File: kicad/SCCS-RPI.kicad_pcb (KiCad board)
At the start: 4 copper layers, 228 x 122 mm, 298 parts, among them J1 Conn_Coaxial, J2 12VDC IN, K1 Relay_SPDT, K2 Relay_SPDT, K3 Relay_SPDT, K4 Relay_SPDT, Q1 IRLR7843, Q10 IRLR7843, Q11 IRLR7843, Q12 IRLR7843, Q13 IRLR7843, Q14 IRLR7843, Q15 IRLR7843, Q16 IRLR7843, Q17 2N7000, Q18 2N7000, Q19 2N7000, Q2 IRLR7843, Q20 2N7000, Q3 IRLR7843, Q4 IRLR7843, Q5 IRLR7843, Q6 IRLR7843, Q7 IRLR7843, Q8 IRLR7843, Q9 IRLR7843, SW1 RESET, SW2 BOOT, SW3 RESET, SW4 BOOT, U1 SN74LVC2T45DCUR, U2 AP64501SP-13, U3 PC817, U4 PC817, U5 PC817, U6 PC817

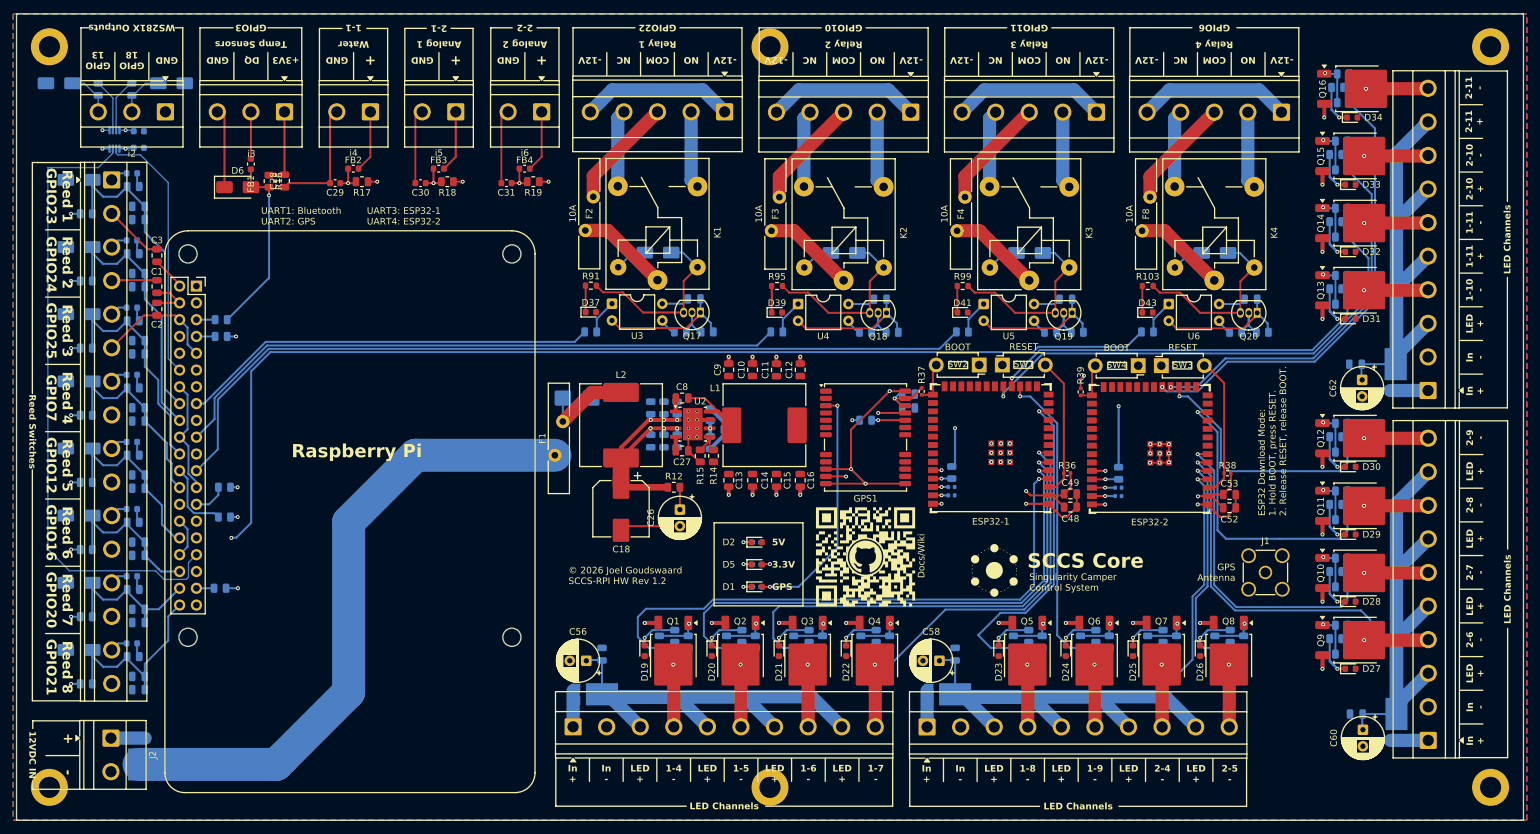
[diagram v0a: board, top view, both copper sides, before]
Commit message: Update SCCS-RPI KiCad design and production files
Add GPS RF ESD and matching (ESD103-B1-02EL, 27nH, 10R, 100nF),
swap the 10A fuses to A16-1000, retune copper zone fills, and
regenerate BOM, positions, netlist, gerbers, and schematics PDF.
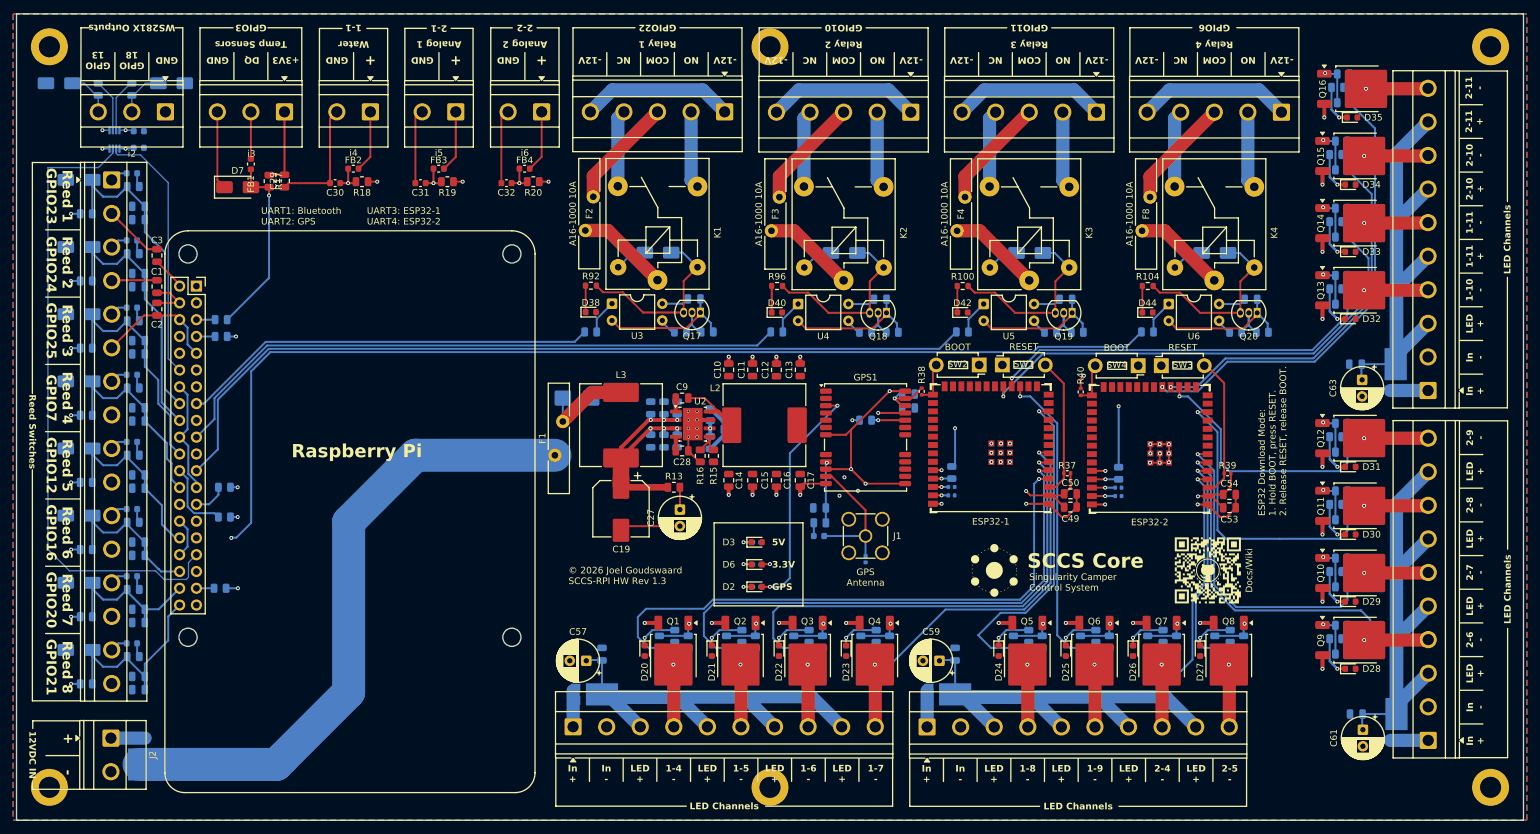
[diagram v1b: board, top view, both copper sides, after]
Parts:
- added C8: 100nF, Capacitor_SMD:C_0805_2012Metric, B.Cu at (322.0, 200.8)
- added D1: ESD103-B1-02EL, Diode_SMD:D_0402_1005Metric, B.Cu at (329.0, 208.5)
- added L1: 27nH, Inductor_SMD:L_0603_1608Metric, B.Cu at (321.9, 205.0)
- added R8: 10R, Resistor_SMD:R_0805_2012Metric, B.Cu at (322.0, 203.0)
- F1, F2, F3, F4, F5: value 10A -> A16-1000 10A
- moved J1 60.8 mm to (329.0, 205.0)
- moved G*** 51.8 mm to (380.8, 210.2)
- renumbered C9 to C10, C10 to C11, C11 to C12, C12 to C13, C13 to C14, C14 to C15, C15 to C16, C16 to C17, C17 to C18, C18 to C19, C19 to C20, C20 to C21, C21 to C22, C22 to C23, C23 to C24, C24 to C25, C25 to C26, C26 to C27, C27 to C28, C28 to C29, C29 to C30, C30 to C31, C31 to C32, C32 to C33, C33 to C34, C34 to C35, C35 to C36, C36 to C37, C37 to C38, C38 to C39, C39 to C40, C40 to C41, C41 to C42, C42 to C43, C43 to C44, C44 to C45, C45 to C46, C46 to C47, C47 to C48, C48 to C49, C49 to C50, C50 to C51, C51 to C52, C52 to C53, C53 to C54, C54 to C55, C55 to C56, C56 to C57, C57 to C58, C58 to C59, C59 to C60, C60 to C61, C61 to C62, C62 to C63, C63 to C64, C64 to C65, C65 to C66, C66 to C67, C67 to C68, C8 to C9, D9 to D10, D10 to D11, D11 to D12, D12 to D13, D13 to D14, D14 to D15, D15 to D16, D16 to D17, D17 to D18, D18 to D19, D1 to D2, D19 to D20, D20 to D21, D21 to D22, D22 to D23, D23 to D24, D24 to D25, D25 to D26, D26 to D27, D27 to D28, D28 to D29, D2 to D3, D29 to D30, D30 to D31, D31 to D32, D32 to D33, D33 to D34, D34 to D35, D35 to D36, D36 to D37, D37 to D38, D38 to D39, D3 to D4, D39 to D40, D40 to D41, D41 to D42, D42 to D43, D43 to D44, D44 to D45, D4 to D5, D5 to D6, D6 to D7, D7 to D8, D8 to D9, L1 to L2, L2 to L3, R9 to R10, R99 to R100, R100 to R101, R101 to R102, R102 to R103, R103 to R104, R104 to R105, R105 to R106, R10 to R11, R11 to R12, R12 to R13, R13 to R14, R14 to R15, R15 to R16, R16 to R17, R17 to R18, R18 to R19, R19 to R20, R20 to R21, R21 to R22, R22 to R23, R23 to R24, R24 to R25, R25 to R26, R26 to R27, R27 to R28, R28 to R29, R29 to R30, R30 to R31, R31 to R32, R32 to R33, R33 to R34, R34 to R35, R35 to R36, R36 to R37, R37 to R38, R38 to R39, R39 to R40, R40 to R41, R41 to R42, R42 to R43, R43 to R44, R44 to R45, R45 to R46, R46 to R47, R47 to R48, R48 to R49, R49 to R50, R50 to R51, R51 to R52, R52 to R53, R53 to R54, R54 to R55, R55 to R56, R56 to R57, R57 to R58, R58 to R59, R59 to R60, R60 to R61, R61 to R62, R62 to R63, R63 to R64, R64 to R65, R65 to R66, R66 to R67, R67 to R68, R68 to R69, R69 to R70, R70 to R71, R71 to R72, R72 to R73, R73 to R74, R74 to R75, R75 to R76, R76 to R77, R77 to R78, R78 to R79, R79 to R80, R80 to R81, R81 to R82, R82 to R83, R83 to R84, R84 to R85, R85 to R86, R86 to R87, R87 to R88, R88 to R89, R8 to R9, R89 to R90, R90 to R91, R91 to R92, R92 to R93, R93 to R94, R94 to R95, R95 to R96, R96 to R97, R97 to R98, R98 to R99
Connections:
- GPS1 pad 7: unconnected-(GPS1-VDD_USB-Pad7) -> GND
- GPS1 pad 9: unconnected-(GPS1-VCC_RF-Pad9) -> Net-(GPS1-VCC_RF)
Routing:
- net Net-(D1-A2): track 72.5 -> 21.3 mm, vias 1 -> 0
- net Net-(GPS1-VCC_RF): track 0.00 -> 9.15 mm, vias 0 -> 1
- net GND: track 326.4 -> 330.5 mm, vias 50 -> 52
- net Net-(L1-Pad1): track 0.00 -> 2.00 mm
- net Net-(D2-A): track 37.1 -> 35.6 mm
- net +5V: vias 1 -> 2
- added copper zone on In1.Cu, net GND
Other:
- board text added: "© 2026 Joel Goudswaard SCCS-RPI HW Rev 1.3"
- board text removed: "© 2026 Joel Goudswaard SCCS-RPI HW Rev 1.2"
